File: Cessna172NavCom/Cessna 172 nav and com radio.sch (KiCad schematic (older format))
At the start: 18 parts, among them J1 Conn_02x09_Odd_Even, J2 USB_B_Micro, SW1 SW_Push, SW2 SW_Push, SW3 SW_Push

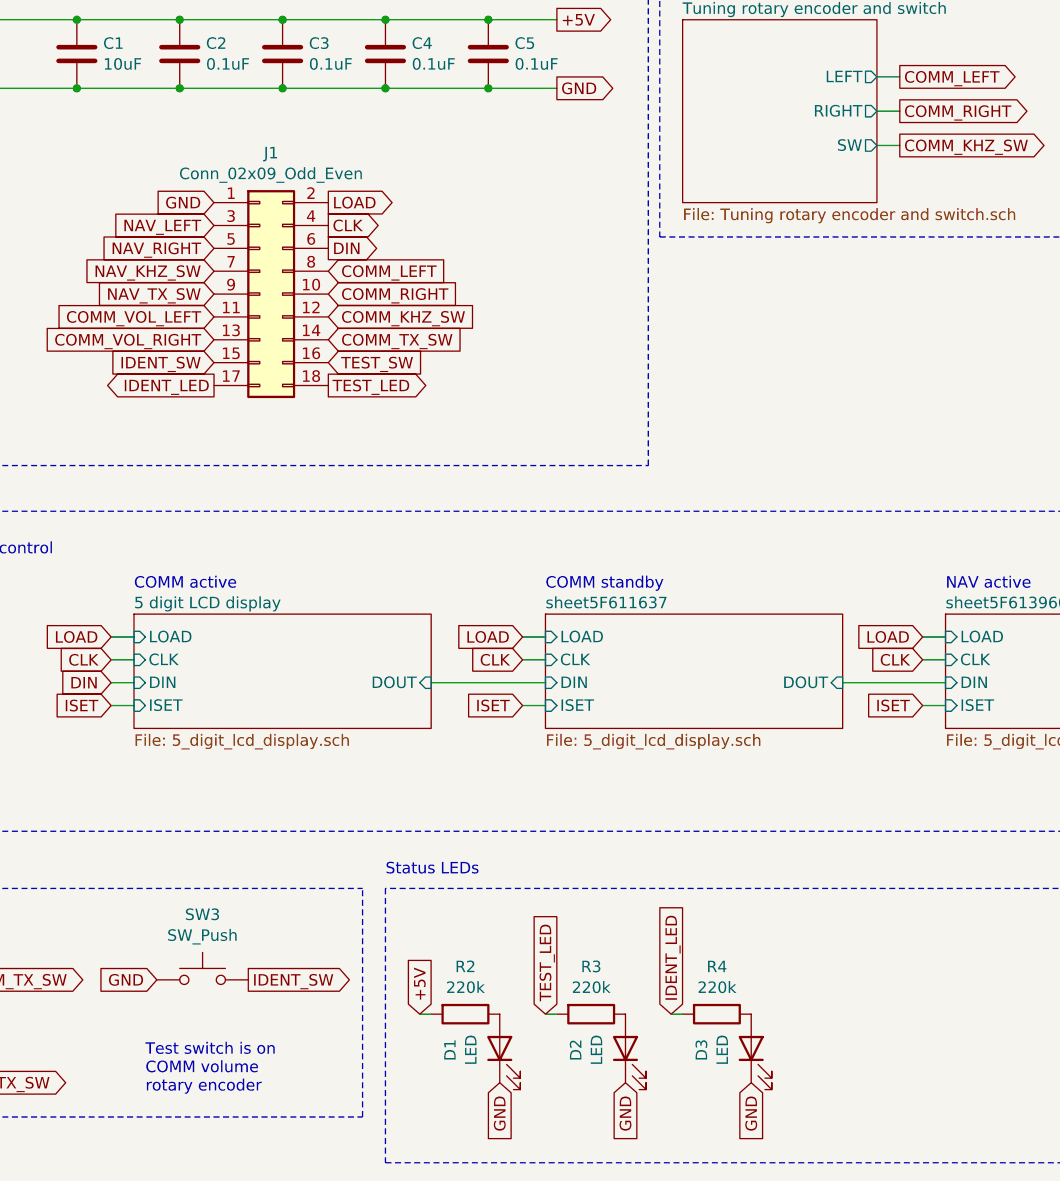
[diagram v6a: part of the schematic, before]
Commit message: Updated rotary encoder with proper footprint
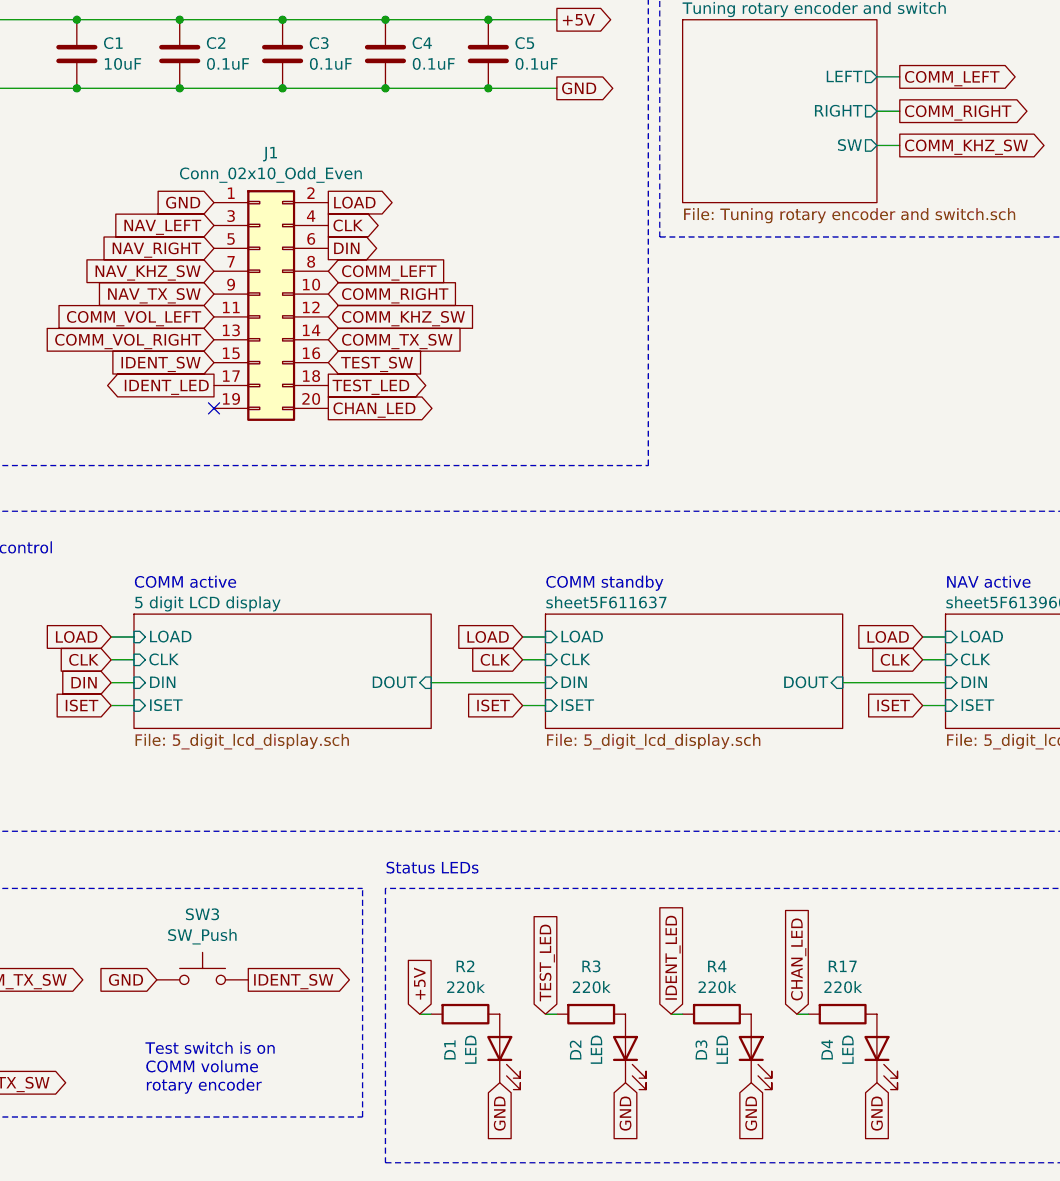
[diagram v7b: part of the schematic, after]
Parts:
- removed J1: Conn_02x09_Odd_Even, symbol Connector_Generic:Conn_02x09_Odd_Even
- added D4: LED, LED_THT:LED_D5.0mm, symbol Device:LED
- added J1: Conn_02x10_Odd_Even, Connector_PinHeader_2.54mm:PinHeader_2x10_P2.54mm_Vertical, symbol Connector_Generic:Conn_02x10_Odd_Even
- added R17: 220k, Resistor_SMD:R_0805_2012Metric_Pad1.15x1.40mm_HandSolder, symbol Device:R
- J2: footprint (none) -> Connector_USB:USB_Micro-B_Molex-105017-0001
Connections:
- net CLK: now also J1.4 (Pin_4)
- net COMM_KHZ_SW: now also J1.12 (Pin_12)
- net COMM_LEFT: now also J1.8 (Pin_8)
- net COMM_RIGHT: now also J1.10 (Pin_10)
- net COMM_TX_SW: now also J1.14 (Pin_14)
- net COMM_VOL_LEFT: now also J1.11 (Pin_11)
- net COMM_VOL_RIGHT: now also J1.13 (Pin_13)
- net DIN: now also J1.6 (Pin_6)
- net GND: now also D4.1 (K), J1.1 (Pin_1)
- net IDENT_LED: now also J1.17 (Pin_17)
- net IDENT_SW: now also J1.15 (Pin_15)
- net LOAD: now also J1.2 (Pin_2)
- net NAV_KHZ_SW: now also J1.7 (Pin_7)
- net NAV_LEFT: now also J1.3 (Pin_3)
- net NAV_RIGHT: now also J1.5 (Pin_5)
- net NAV_TX_SW: now also J1.9 (Pin_9)
- net TEST_LED: now also J1.18 (Pin_18)
- net TEST_SW: now also J1.16 (Pin_16)
- new net: D4.2 (A), R17.1
- new net CHAN_LED: J1.20 (Pin_20), R17.2
- no-connect marks 6 -> 7
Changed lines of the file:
@@
 F 0 "J2" H 1050 500 50  0000 C CNN
 F 1 "USB_B_Micro" H 1050 600 50  0000 C CNN
-F 2 "" H 1200 1050 50  0001 C CNN
+F 2 "Connector_USB:USB_Micro-B_Molex-105017-0001" H 1200 1050 50  0001 C CNN
 F 3 "~" H 1200 1050 50  0001 C CNN
 	1    1050 1100
@@
 Wire Wire Line
 	3650 1200 3950 1200
+Text GLabel 2450 1700 0    50   Input ~ 0
+GND
+NoConn ~ 8900 3800
 $Comp
-L Connector_Generic:Conn_02x09_Odd_Even J1
-U 1 1 5F645ECE
+L Device:LED D4
+U 1 1 5F679E44
+P 5350 5400
+F 0 "D4" H 5343 5616 50  0000 C CNN
+F 1 "LED" H 5343 5525 50  0000 C CNN
+F 2 "LED_THT:LED_D5.0mm" H 5350 5400 50  0001 C CNN
+F 3 "~" H 5350 5400 50  0001 C CNN
+	1    5350 5400
+	0    -1   -1   0
+$EndComp
+Text GLabel 5350 5550 3    50   Input ~ 0
+GND
+Text GLabel 5000 5250 1    50   Input ~ 0
+CHAN_LED
+$Comp
+L Device:R R17
+U 1 1 5F679E4C
+P 5200 5250
+F 0 "R17" V 4993 5250 50  0000 C CNN
+F 1 "220k" V 5084 5250 50  0000 C CNN
+F 2 "Resistor_SMD:R_0805_2012Metric_Pad1.15x1.40mm_HandSolder" V 5130 5250 50  0001 C CNN
+F 3 "~" H 5200 5250 50  0001 C CNN
+	1    5200 5250
+	0    1    1    0
+$EndComp
+Wire Wire Line
+	5000 5250 5050 5250
+$Comp
+L Connector_Generic:Conn_02x10_Odd_Even J1
+U 1 1 5F67B4E3
 P 2650 2100
 F 0 "J1" H 2700 2717 50  0000 C CNN
-F 1 "Conn_02x09_Odd_Even" H 2700 2626 50  0000 C CNN
-F 2 "" H 2650 2100 50  0001 C CNN
+F 1 "Conn_02x10_Odd_Even" H 2700 2626 50  0000 C CNN
+F 2 "Connector_PinHeader_2.54mm:PinHeader_2x10_P2.54mm_Vertical" H 2650 2100 50  0001 C CNN
 F 3 "~" H 2650 2100 50  0001 C CNN
 	1    2650 2100
 	1    0    0    -1
 $EndComp
-Text GLabel 2450 1700 0    50   Input ~ 0
-GND
-NoConn ~ 8900 3800
+Text GLabel 2950 2600 2    50   Output ~ 0
+CHAN_LED
+NoConn ~ 2450 2600
 $EndSCHEMATC

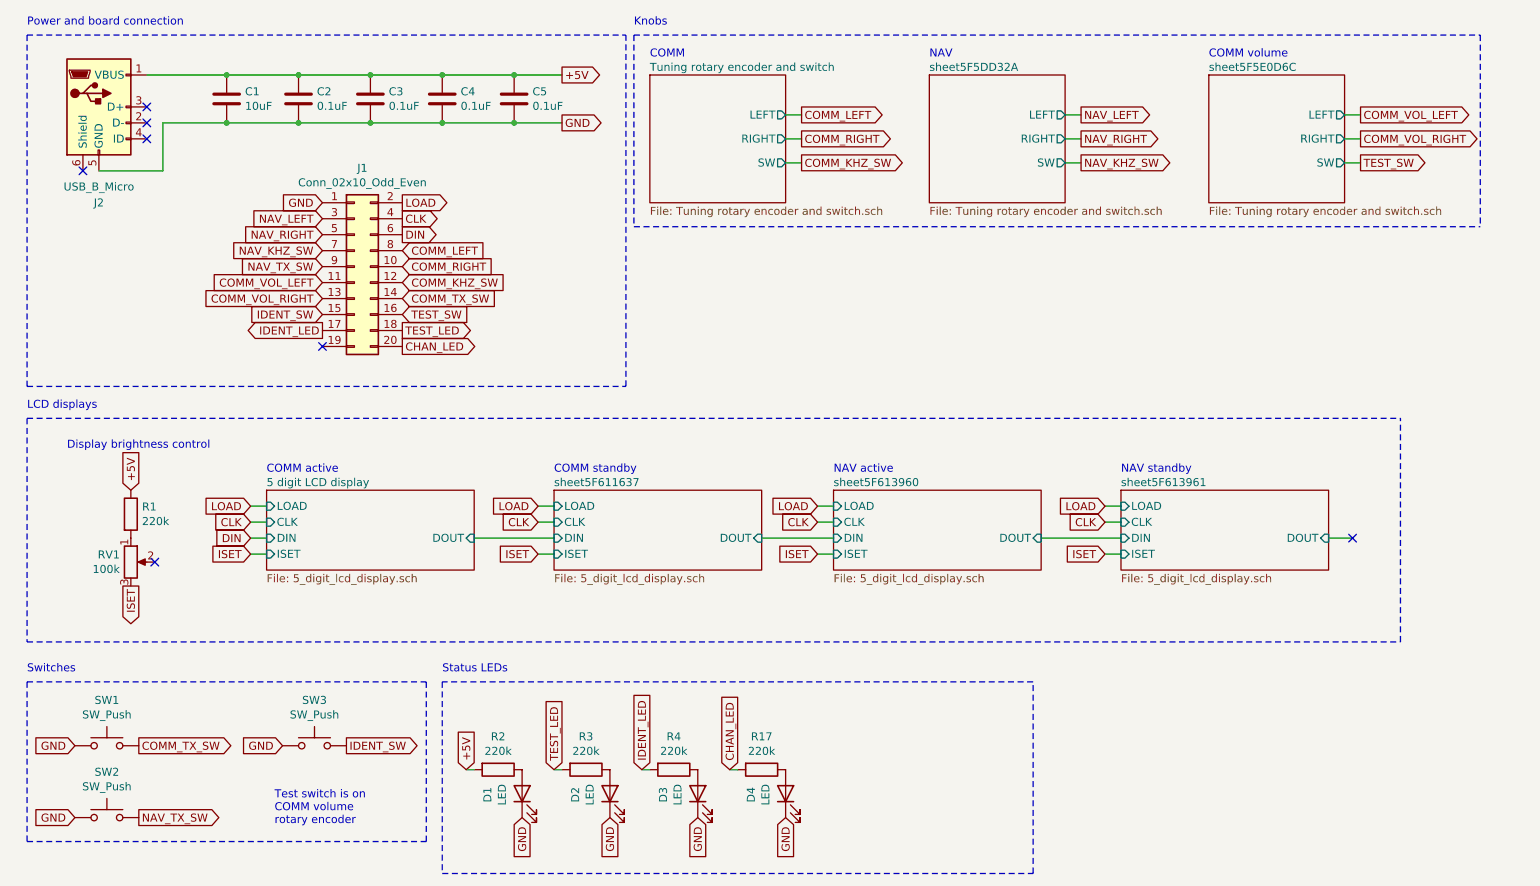
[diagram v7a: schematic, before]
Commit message: Connection, footprint, and layout updates
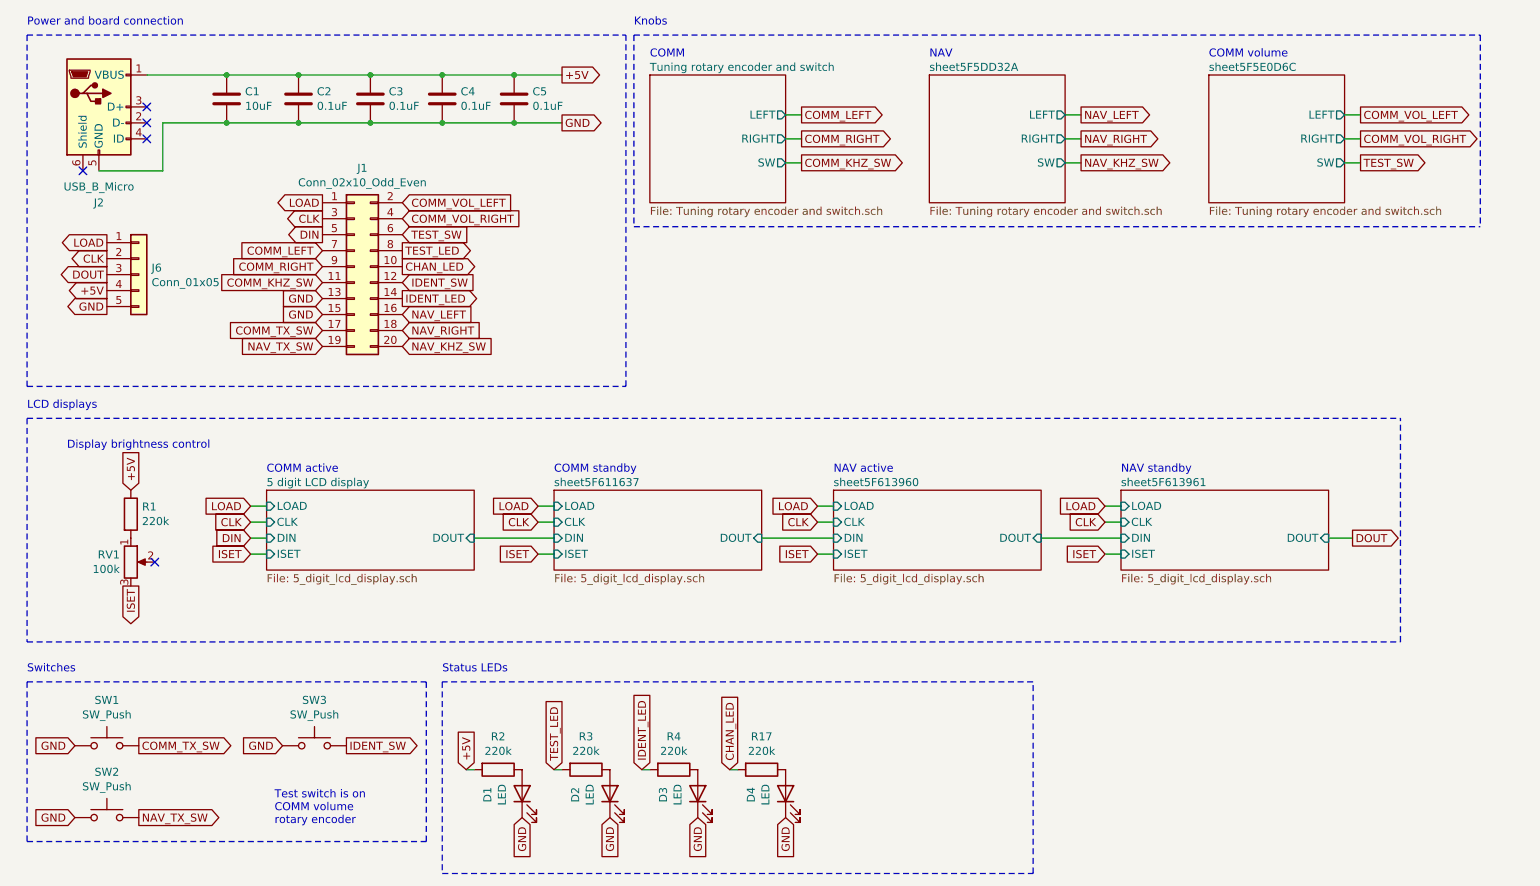
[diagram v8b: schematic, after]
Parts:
- added J6: Conn_01x05, Connector_PinHeader_2.54mm:PinHeader_1x05_P2.54mm_Vertical, symbol Connector_Generic:Conn_01x05
- RV1: footprint Potentiometer_THT:Potentiometer_Piher_PT-10-V10_Vertical_Hole -> Cessna 172 nav and com radio:A-2506 trimpot resistor
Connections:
- net +5V: now also J6.4 (Pin_4)
- net CHAN_LED: now also J1.10 (Pin_10); no longer J1.20 (Pin_20)
- net CLK: now also J1.3 (Pin_3), J6.2 (Pin_2); no longer J1.4 (Pin_4)
- net COMM_KHZ_SW: now also J1.11 (Pin_11); no longer J1.12 (Pin_12)
- net COMM_LEFT: now also J1.7 (Pin_7); no longer J1.8 (Pin_8)
- net COMM_RIGHT: now also J1.9 (Pin_9); no longer J1.10 (Pin_10)
- net COMM_TX_SW: now also J1.17 (Pin_17); no longer J1.14 (Pin_14)
- net COMM_VOL_LEFT: now also J1.2 (Pin_2); no longer J1.11 (Pin_11)
- net COMM_VOL_RIGHT: now also J1.4 (Pin_4); no longer J1.13 (Pin_13)
- net DIN: now also J1.5 (Pin_5); no longer J1.6 (Pin_6)
- net GND: now also J1.13 (Pin_13), J1.15 (Pin_15), J6.5 (Pin_5); no longer J1.1 (Pin_1)
- net IDENT_LED: now also J1.14 (Pin_14); no longer J1.17 (Pin_17)
- net IDENT_SW: now also J1.12 (Pin_12); no longer J1.15 (Pin_15)
- net LOAD: now also J1.1 (Pin_1), J6.1 (Pin_1); no longer J1.2 (Pin_2)
- net NAV_KHZ_SW: now also J1.20 (Pin_20); no longer J1.7 (Pin_7)
- net NAV_LEFT: now also J1.16 (Pin_16); no longer J1.3 (Pin_3)
- net NAV_RIGHT: now also J1.18 (Pin_18); no longer J1.5 (Pin_5)
- net NAV_TX_SW: now also J1.19 (Pin_19); no longer J1.9 (Pin_9)
- net TEST_LED: now also J1.8 (Pin_8); no longer J1.18 (Pin_18)
- net TEST_SW: now also J1.6 (Pin_6); no longer J1.16 (Pin_16)
- new net DOUT: J6.3 (Pin_3)
- no-connect marks 7 -> 5
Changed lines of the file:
@@
 Comment4 ""
 $EndDescr
-Text GLabel 2950 1700 2    50   Output ~ 0
+Text GLabel 2450 1700 0    50   Output ~ 0
 LOAD
-Text GLabel 2950 1800 2    50   Output ~ 0
+Text GLabel 2450 1800 0    50   Output ~ 0
 CLK
-Text GLabel 2950 1900 2    50   Output ~ 0
+Text GLabel 2450 1900 0    50   Output ~ 0
 DIN
 $Comp
@@
 Text Notes 600  3000 0    50   ~ 0
 LCD displays
-Text GLabel 2950 2000 2    50   Input ~ 0
+Text GLabel 2450 2000 0    50   Input ~ 0
 COMM_LEFT
-Text GLabel 2950 2100 2    50   Input ~ 0
+Text GLabel 2450 2100 0    50   Input ~ 0
 COMM_RIGHT
 Text Notes 4500 800  0    50   ~ 0
@@
 F4 "SW" O R 5350 1450 50
 $EndSheet
-Text GLabel 2950 2200 2    50   Input ~ 0
+Text GLabel 2450 2200 0    50   Input ~ 0
 COMM_KHZ_SW
 Text Notes 6250 800  0    50   ~ 0
@@
 F4 "SW" O R 7100 1450 50
 $EndSheet
-Text GLabel 2450 1800 0    50   Input ~ 0
+Text GLabel 2950 2400 2    50   Input ~ 0
 NAV_LEFT
-Text GLabel 2450 1900 0    50   Input ~ 0
+Text GLabel 2950 2500 2    50   Input ~ 0
 NAV_RIGHT
 Wire Notes Line
@@
 Text Notes 4400 600  0    50   ~ 0
 Knobs
-Text GLabel 2950 2300 2    50   Input ~ 0
+Text GLabel 2450 2500 0    50   Input ~ 0
 COMM_TX_SW
-Text GLabel 2450 2100 0    50   Input ~ 0
+Text GLabel 2450 2600 0    50   Input ~ 0
 NAV_TX_SW
 Wire Wire Line
 	7100 1450 7200 1450
-Text GLabel 2450 2000 0    50   Input ~ 0
+Text GLabel 2950 2600 2    50   Input ~ 0
 NAV_KHZ_SW
 $Comp
@@
 Wire Notes Line
 	4400 650  9700 650
-Text GLabel 2950 2400 2    50   Input ~ 0
+Text GLabel 2950 1900 2    50   Input ~ 0
 TEST_SW
-Text GLabel 2950 2500 2    50   Output ~ 0
+Text GLabel 2950 2000 2    50   Output ~ 0
 TEST_LED
-Text GLabel 2450 2200 0    50   Input ~ 0
+Text GLabel 2950 1700 2    50   Input ~ 0
 COMM_VOL_LEFT
-Text GLabel 2450 2300 0    50   Input ~ 0
+Text GLabel 2950 1800 2    50   Input ~ 0
 COMM_VOL_RIGHT
-Text GLabel 2450 2400 0    50   Input ~ 0
+Text GLabel 2950 2200 2    50   Input ~ 0
 IDENT_SW
-Text GLabel 2450 2500 0    50   Output ~ 0
+Text GLabel 2950 2300 2    50   Output ~ 0
 IDENT_LED
 Wire Notes Line
@@
 F 0 "RV1" H 1181 3996 50  0000 R CNN
 F 1 "100k" H 1181 3905 50  0000 R CNN
-F 2 "Potentiometer_THT:Potentiometer_Piher_PT-10-V10_Vertical_Hole" H 1250 3950 50  0001 C CNN
+F 2 "Cessna 172 nav and com radio:A-2506 trimpot resistor" H 1250 3950 50  0001 C CNN
 F 3 "~" H 1250 3950 50  0001 C CNN
 	1    1250 3950
@@
 Wire Wire Line
 	3650 1200 3950 1200
-Text GLabel 2450 1700 0    50   Input ~ 0
-GND
-NoConn ~ 8900 3800
+Text GLabel 2450 2300 0    50   Input ~ 0
+GND
 $Comp
 L Device:LED D4
@@
 	1    0    0    -1
 $EndComp
-Text GLabel 2950 2600 2    50   Output ~ 0
+Text GLabel 2950 2100 2    50   Output ~ 0
 CHAN_LED
-NoConn ~ 2450 2600
+Text GLabel 2450 2400 0    50   Input ~ 0
+GND
+Text GLabel 1100 1950 0    50   Output ~ 0
+LOAD
+Text GLabel 1100 2050 0    50   Output ~ 0
+CLK
+Text GLabel 1100 2150 0    50   Output ~ 0
+DOUT
+Text GLabel 8900 3800 2    50   Output ~ 0
+DOUT
+$Comp
+L Connector_Generic:Conn_01x05 J6
+U 1 1 5F64CCD1
+P 1300 2150
+F 0 "J6" H 1380 2192 50  0000 L CNN
+F 1 "Conn_01x05" H 1380 2101 50  0000 L CNN
+F 2 "Connector_PinHeader_2.54mm:PinHeader_1x05_P2.54mm_Vertical" H 1300 2150 50  0001 C CNN
+F 3 "~" H 1300 2150 50  0001 C CNN
+	1    1300 2150
+	1    0    0    -1
+$EndComp
+Text GLabel 1100 2250 0    50   Output ~ 0
++5V
+Text GLabel 1100 2350 0    50   Output ~ 0
+GND
 $EndSCHEMATC
